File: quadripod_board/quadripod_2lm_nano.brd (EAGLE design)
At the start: 50.5 x 86.4 mm, 8 parts

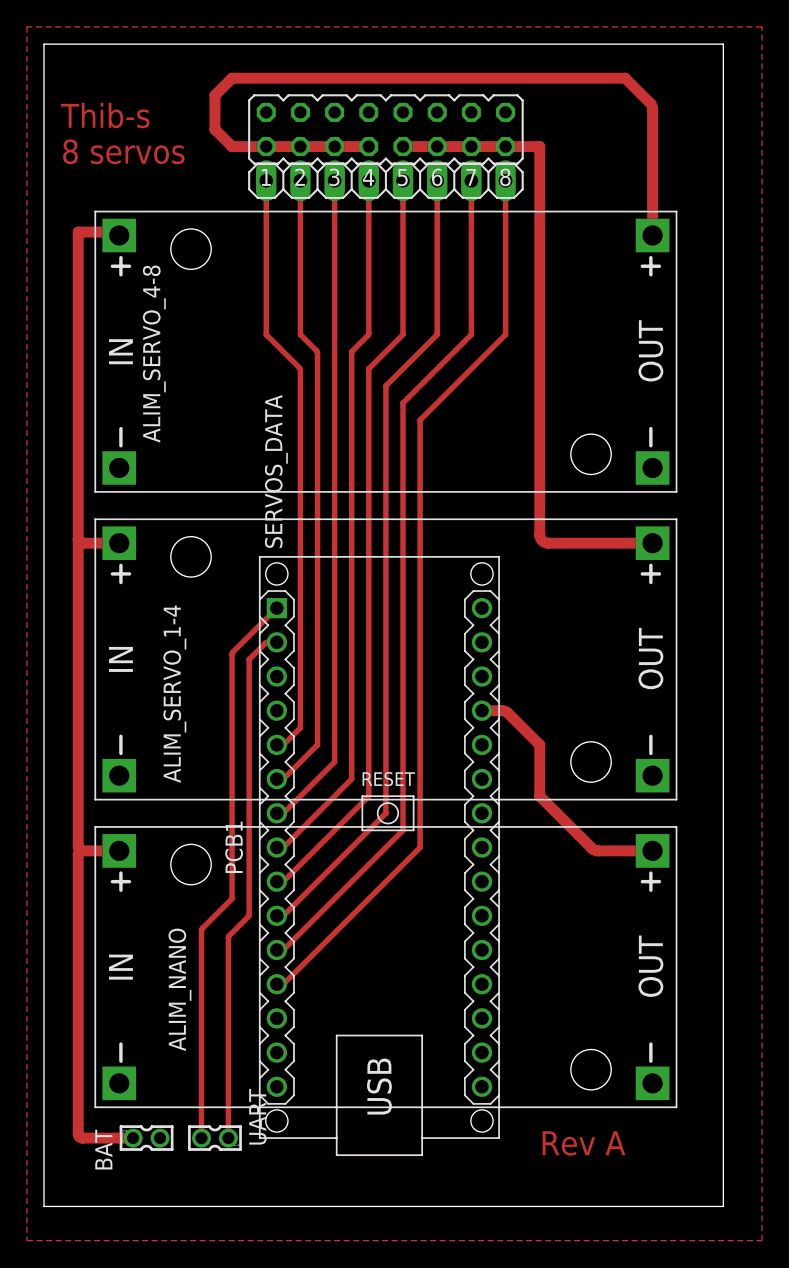
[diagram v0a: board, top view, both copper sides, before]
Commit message: board revision, added diodes to avoid powering the servos while programming the arduino
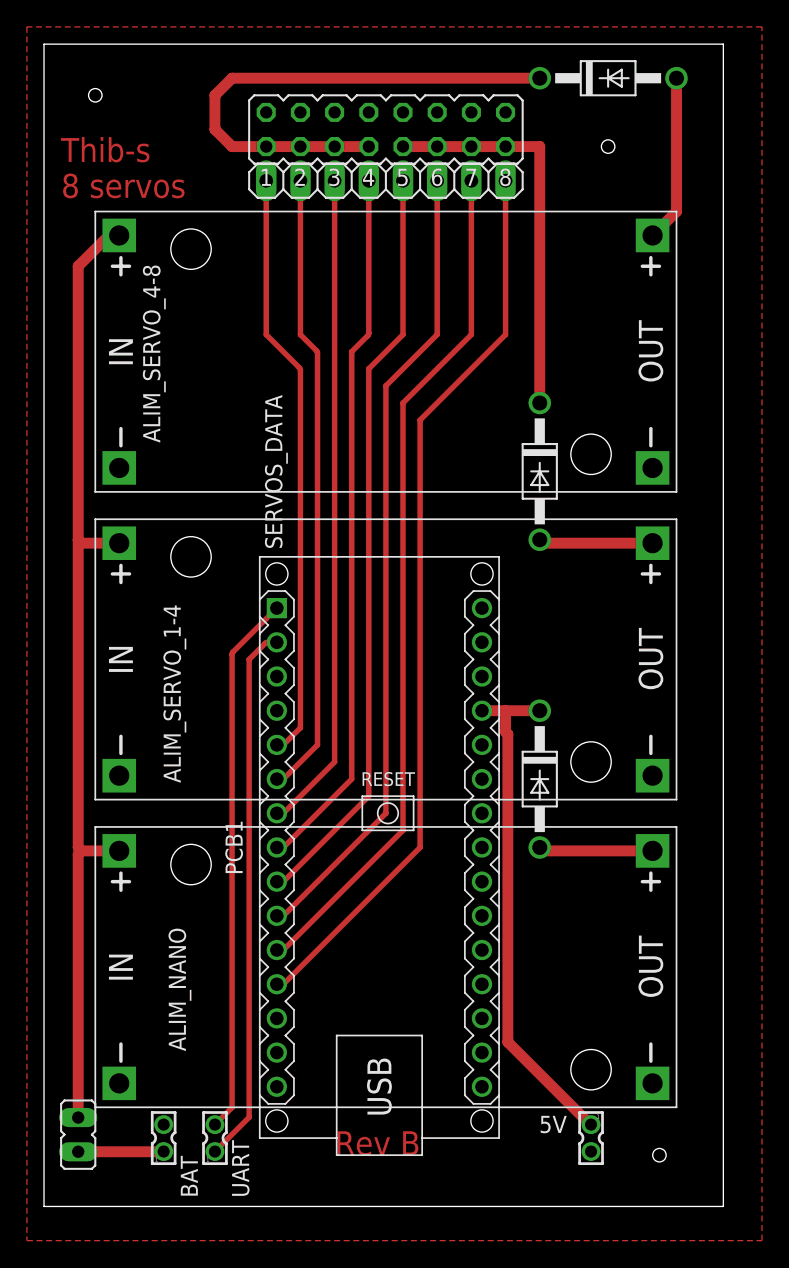
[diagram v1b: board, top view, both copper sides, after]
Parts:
- added 5V: (no value), con-garry:332-02
- added D1, D2, D3: 1N4004, diode:DO41-10
- added JP1: (no value), jumper:JP1
- moved BAT 1.27 mm to (14.0, 2.54), turned to 0 degrees
- turned UART to 0 degrees
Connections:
- new net N$1: ALIM_SERVO_4-8.OUT+, D3.A
- new net N$15: ALIM_NANO.IN+, ALIM_SERVO_1-4.IN+, ALIM_SERVO_4-8.IN+, JP1.2
- new net N$3: 5V.1, D2.C, PCB1.J2.4
- new net N$4: ALIM_SERVO_1-4.OUT+, D1.A
- net +12V: now also JP1.1; no longer ALIM_NANO.IN+, ALIM_SERVO_1-4.IN+, ALIM_SERVO_4-8.IN+
- net 5V_NANO: now also D2.A; no longer PCB1.J2.4
- net 5V_S1-4: now also D3.C; no longer ALIM_SERVO_4-8.OUT+
- net 5V_S5-8: now also D1.C; no longer ALIM_SERVO_1-4.OUT+
- net GND: now also 5V.2
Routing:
- net +12V: track 80.5 -> 6.36 mm
- net N$15: track 0.00 -> 73.4 mm
- net N$3: track 0.00 -> 37.8 mm
- net 5V_S1-4: track 58.0 -> 39.2 mm
- net 5V_S5-8: track 47.6 -> 29.2 mm
- net N$1: track 0.00 -> 12.4 mm
- net 5V_NANO: track 19.1 -> 8.49 mm
- net N$4: track 0.00 -> 8.49 mm
- net N$13: track 38.7 -> 40.2 mm
- net N$14: track 41.7 -> 40.3 mm
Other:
- board text added: "Rev B"
- board text removed: "Rev A"
